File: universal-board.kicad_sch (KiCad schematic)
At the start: 17 parts, among them J1 USB_C_Receptacle, J2 CONN_I2C_GROVE, J3 CONN_WS2812, SW1 SW_RESET, U1 USBLC6-2SC6, U2 USBLC6-2SC6, U3 ESP32-S3-WROOM-1, U4 AMS1117-3.3

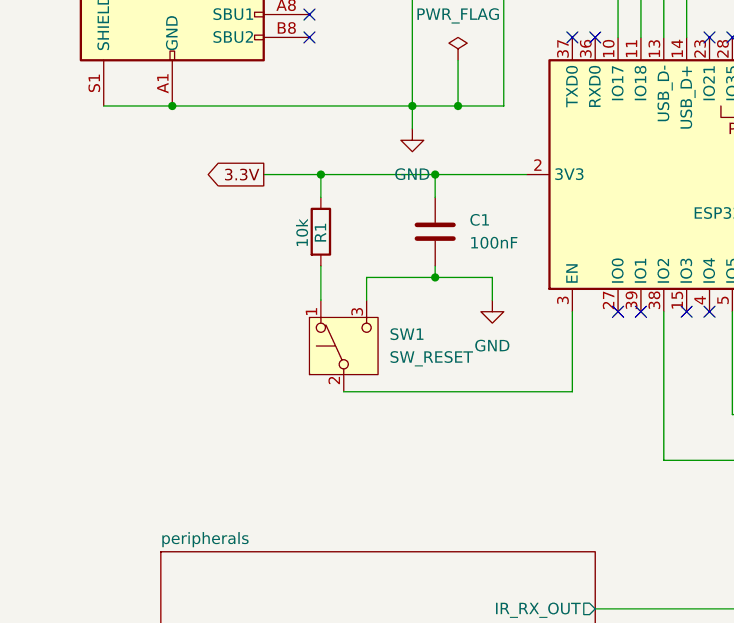
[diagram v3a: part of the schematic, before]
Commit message: Added capacitor for ESP32/EN pin
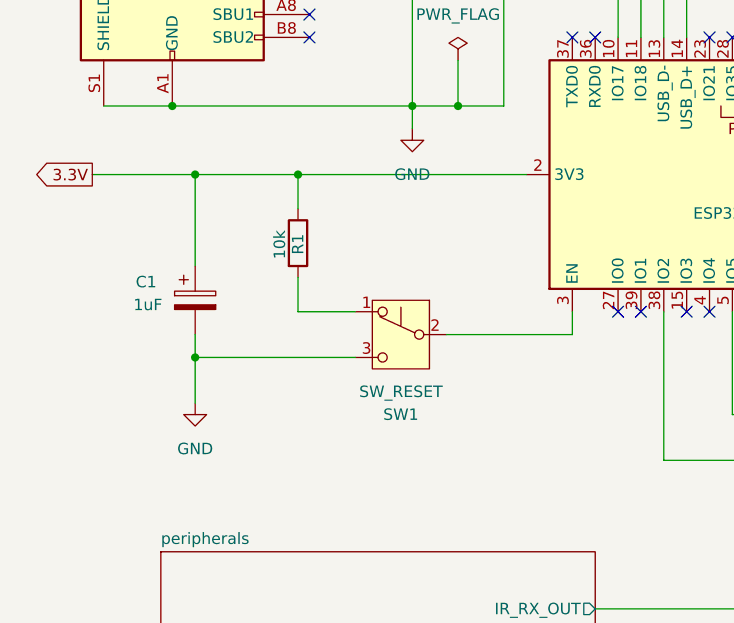
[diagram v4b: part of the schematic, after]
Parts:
- removed C1: 100nF, symbol Device:C
- added C1: 1uF, symbol Device:C_Polarized
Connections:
- net 3.3V: now also C1.1
- net GND: now also C1.2
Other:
- moved on the sheet: R1, SW1

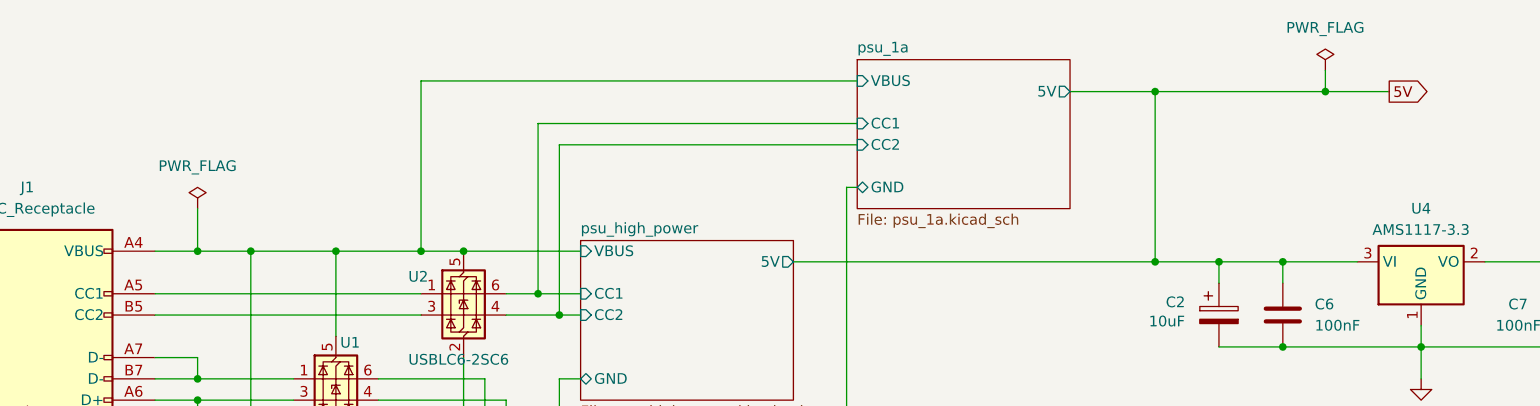
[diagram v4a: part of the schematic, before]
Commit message: Moved some components around for better readability.
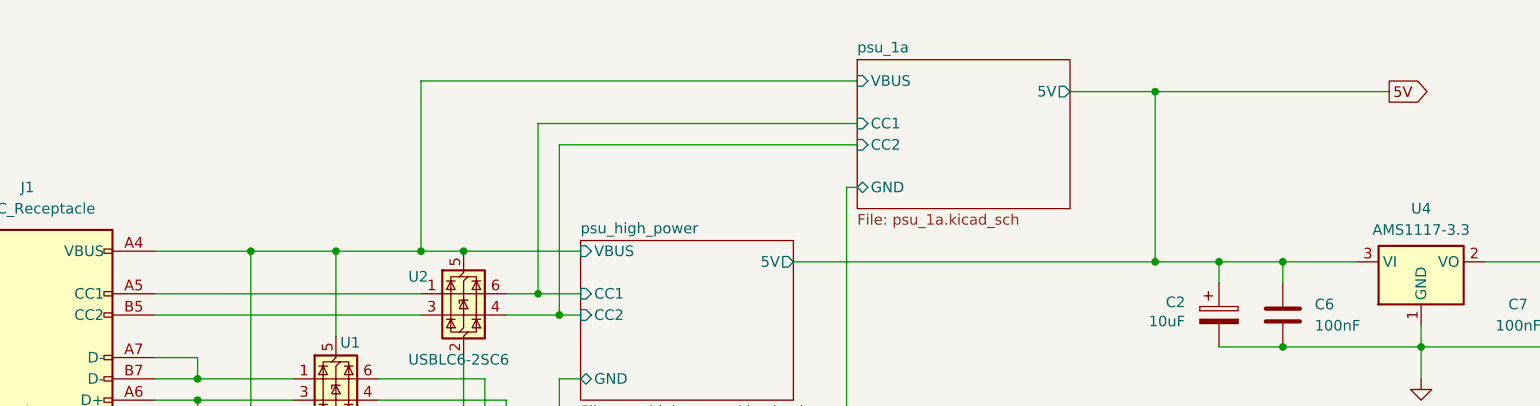
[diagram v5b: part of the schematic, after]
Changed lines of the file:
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@@
-	)
-	(junction
-		(at 185.42 21.59)
-		(diameter 0)
-		(color 0 0 0 0)
 	)
 	(junction
@@
 	)
 	(junction
-		(at 50.8 40.64)
-		(diameter 0)
-		(color 0 0 0 0)
-	)
-	(junction
 		(at 50.8 55.88)
 		(diameter 0)
@@
 	(wire
 		(pts
-			(xy 185.42 21.59) (xy 193.04 21.59)
+			(xy 165.1 21.59) (xy 193.04 21.59)
 		)
 		(stroke
@@
 	(wire
 		(pts
-			(xy 50.8 40.64) (xy 57.15 40.64)
-		)
-		(stroke
-			(width 0)
-			(type default)
-		)
-	)
-	(wire
-		(pts
 			(xy 154.94 21.59) (xy 165.1 21.59)
 		)
@@
 	(wire
 		(pts
-			(xy 50.8 35.56) (xy 50.8 40.64)
-		)
-		(stroke
-			(width 0)
-			(type default)
-		)
-	)
-	(wire
-		(pts
 			(xy 77.47 173.99) (xy 102.87 173.99)
 		)
@@
 	(wire
 		(pts
-			(xy 185.42 19.05) (xy 185.42 21.59)
-		)
-		(stroke
-			(width 0)
-			(type default)
-		)
-	)
-	(wire
-		(pts
 			(xy 91.44 25.4) (xy 91.44 45.72)
 		)
@@
 	(wire
 		(pts
-			(xy 50.8 40.64) (xy 45.72 40.64)
+			(xy 45.72 40.64) (xy 57.15 40.64)
 		)
 		(stroke
@@
 		(pts
 			(xy 33.02 134.62) (xy 50.8 134.62)
-		)
-		(stroke
-			(width 0)
-			(type default)
-		)
-	)
-	(wire
-		(pts
-			(xy 165.1 21.59) (xy 185.42 21.59)
 		)
 		(stroke
@@
 	)
 	(symbol
-		(lib_id "power:PWR_FLAG")
-		(at 185.42 19.05 0)
-		(unit 1)
-		(exclude_from_sim no)
-		(in_bom yes)
-		(on_board yes)
-		(dnp no)
-		(fields_autoplaced yes)
-		(property "Reference" "#FLG03"
-			(at 185.42 17.145 0)
-			(effects
-				(font
-					(size 1.27 1.27)
-				)
-				(hide yes)
-			)
-		)
-		(property "Value" "PWR_FLAG"
-			(at 185.42 13.97 0)
-			(effects
-				(font
-					(size 1.27 1.27)
-				)
-			)
-		)
-		(property "Footprint" ""
-			(at 185.42 19.05 0)
-			(effects
-				(font
-					(size 1.27 1.27)
-				)
-				(hide yes)
-			)
-		)
-		(property "Datasheet" "~"
-			(at 185.42 19.05 0)
-			(effects
-				(font
-					(size 1.27 1.27)
-				)
-				(hide yes)
-			)
-		)
-		(property "Description" "Special symbol for telling ERC where power comes from"
-			(at 185.42 19.05 0)
-			(effects
-				(font
-					(size 1.27 1.27)
-				)
-				(hide yes)
-			)
-		)
-		(pin "1"
-		)
-		(instances
-			(project ""
-				(path "/64404f27-cfd6-41d9-8edb-810ebab8cc14"
-					(reference "#FLG03")
-					(unit 1)
-				)
-			)
-		)
-	)
-	(symbol
 		(lib_id "Connector_Generic:Conn_01x03")
 		(at 163.83 173.99 0)
@@
 					(unit 1)
 				)
-			)
-		)
-	)
-	(symbol
-		(lib_id "power:PWR_FLAG")
-		(at 50.8 35.56 0)
-		(unit 1)
-		(exclude_from_sim no)
-		(in_bom yes)
-		(on_board yes)
-		(dnp no)
-		(fields_autoplaced yes)
-		(property "Reference" "#FLG01"
-			(at 50.8 33.655 0)
-			(effects
-				(font
-					(size 1.27 1.27)
-				)
-				(hide yes)
-			)
-		)
-		(property "Value" "PWR_FLAG"
-			(at 50.8 30.48 0)
-			(effects
-				(font
-					(size 1.27 1.27)
-				)
-			)
-		)
-		(property "Footprint" ""
-			(at 50.8 35.56 0)
-			(effects
-				(font
-					(size 1.27 1.27)
-				)
-				(hide yes)
-			)
-		)
-		(property "Datasheet" "~"
-			(at 50.8 35.56 0)
-			(effects
-				(font
-					(size 1.27 1.27)
-				)
-				(hide yes)
-			)
-		)
-		(property "Description" "Special symbol for telling ERC where power comes from"
-			(at 50.8 35.56 0)
-			(effects
-				(font
-					(size 1.27 1.27)
-				)
-				(hide yes)
-			)
-		)
-		(pin "1"
-		)
-		(instances
-			(project ""
-				(path "/64404f27-cfd6-41d9-8edb-810ebab8cc14"
-					(reference "#FLG01")
-					(unit 1)
-				)

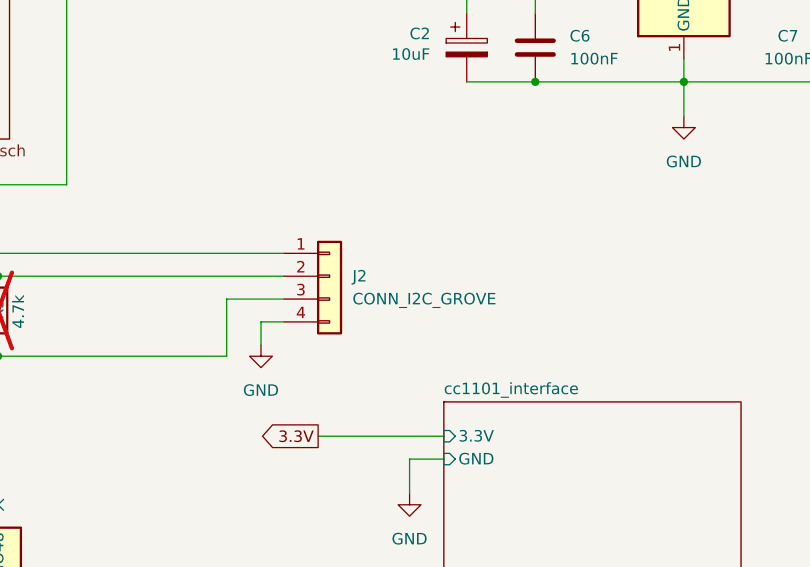
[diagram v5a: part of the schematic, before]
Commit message: Flipped grove connector around
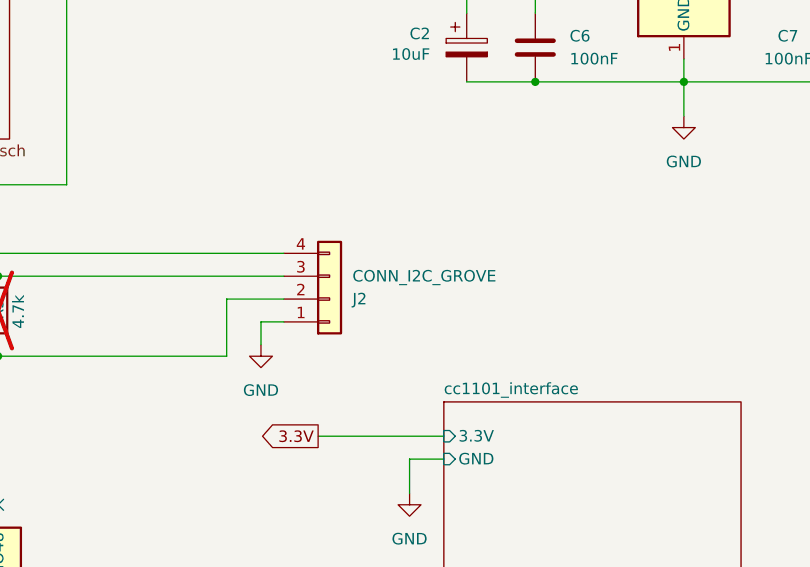
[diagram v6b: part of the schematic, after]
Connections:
- net 3.3V: now also J2.2 (Pin_2); no longer J2.3 (Pin_3)
- net GND: now also J2.1 (Pin_1); no longer J2.4 (Pin_4)
- net at R2.1, U3.10 (IO17): now also J2.4 (Pin_4); no longer J2.1 (Pin_1)
- net at R3.1, U3.11 (IO18): now also J2.3 (Pin_3); no longer J2.2 (Pin_2)
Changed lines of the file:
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@@
 	(symbol
 		(lib_id "Connector_Generic:Conn_01x04")
-		(at 157.48 73.66 0)
+		(at 157.48 76.2 0)
+		(mirror x)
 		(unit 1)
 		(exclude_from_sim no)
@@
 		(on_board yes)
 		(dnp no)
-		(fields_autoplaced yes)
 		(property "Reference" "J2"
-			(at 160.02 73.6599 0)
+			(at 160.02 76.2001 0)
 			(effects
 				(font
@@
 		)
 		(property "Value" "CONN_I2C_GROVE"
-			(at 160.02 76.1999 0)
+			(at 160.02 73.6601 0)
 			(effects
 				(font
@@
 		)
 		(property "Footprint" ""
-			(at 157.48 73.66 0)
+			(at 157.48 76.2 0)
 			(effects
 				(font
@@
 		)
 		(property "Datasheet" "~"
-			(at 157.48 73.66 0)
+			(at 157.48 76.2 0)
 			(effects
 				(font
@@
 		)
 		(property "Description" "Generic connector, single row, 01x04, script generated (kicad-library-utils/schlib/autogen/connector/)"
-			(at 157.48 73.66 0)
+			(at 157.48 76.2 0)
 			(effects
 				(font

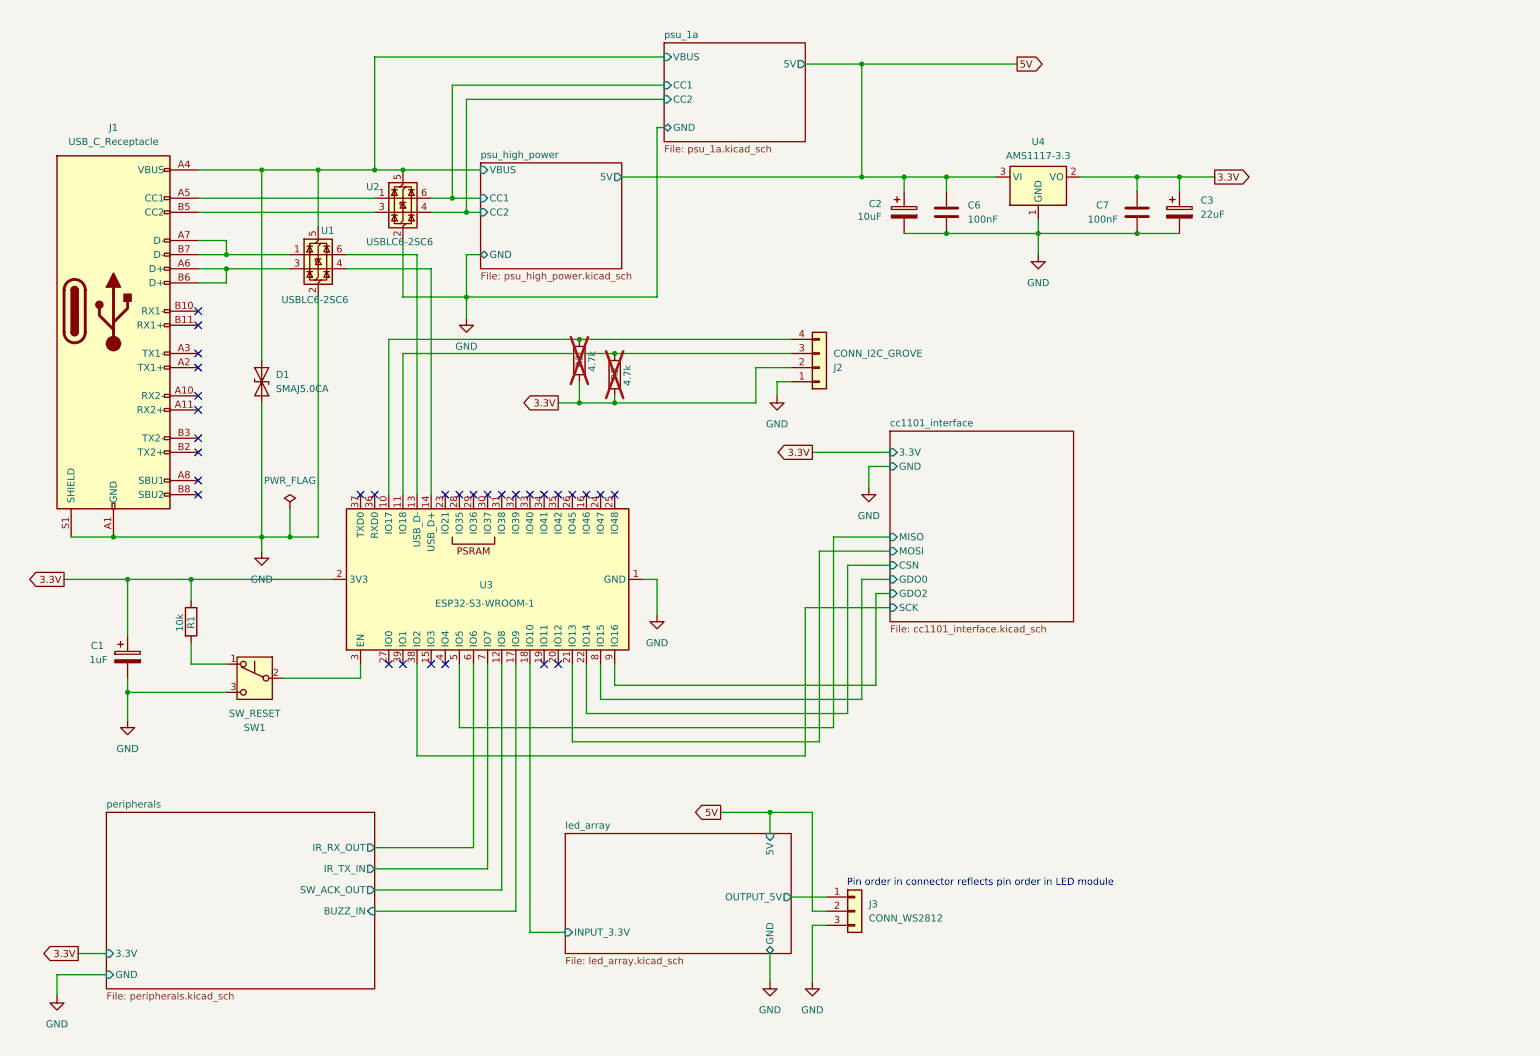
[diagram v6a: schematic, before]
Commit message: Reorganized board to be on one sheet.
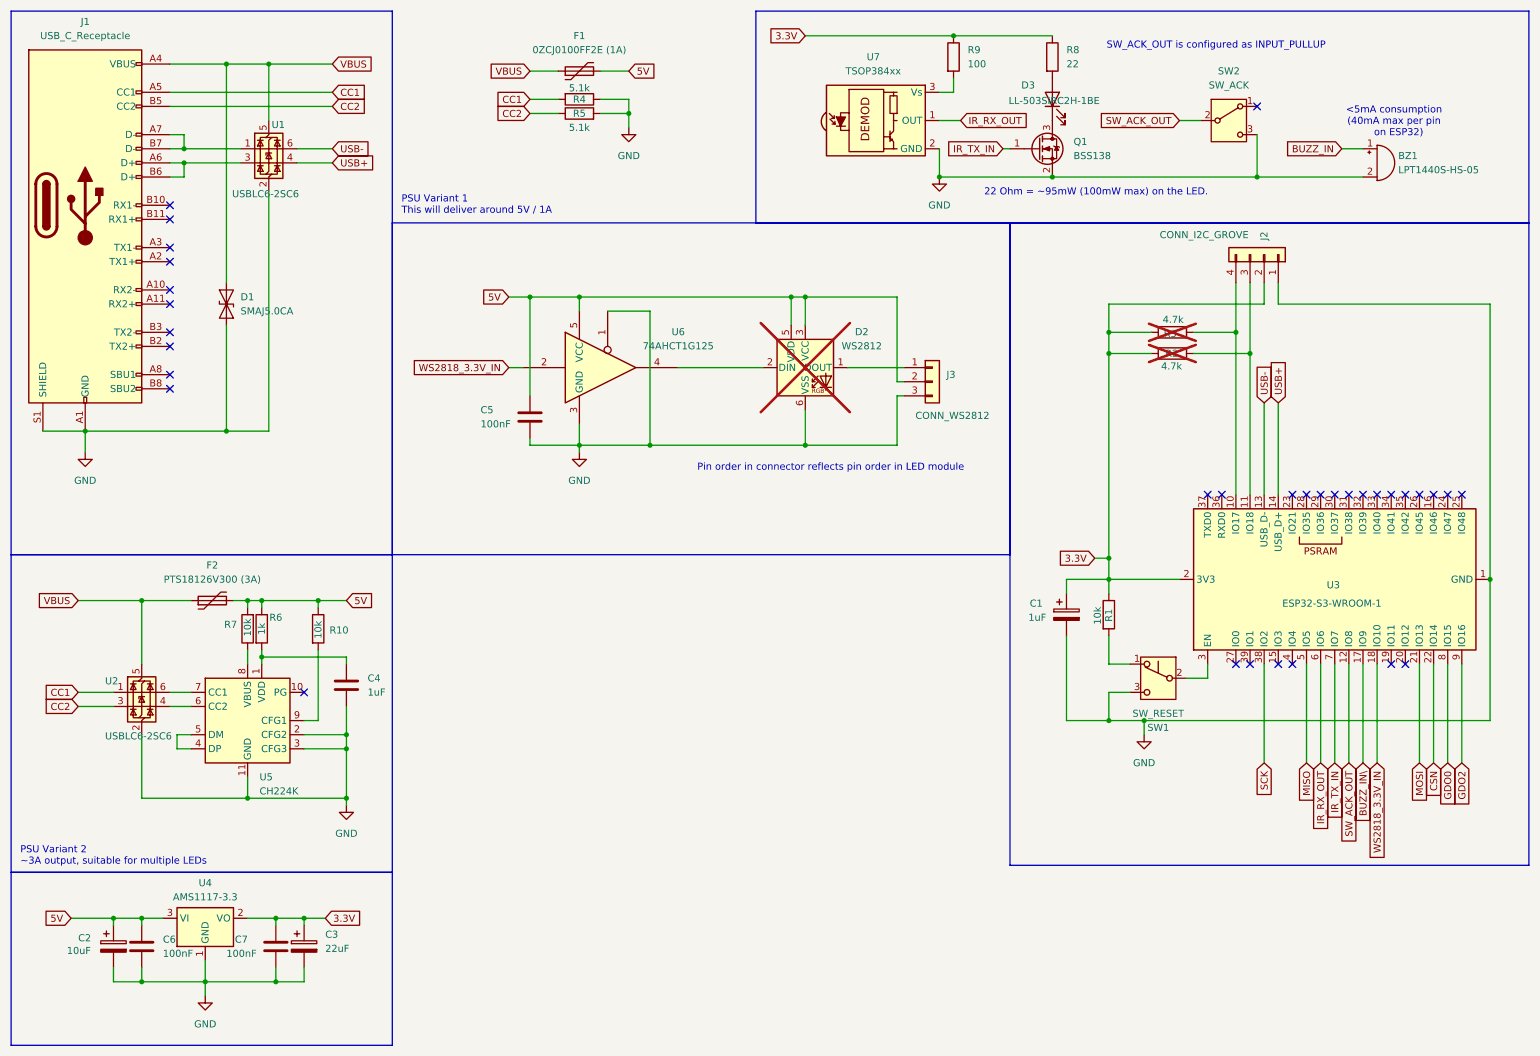
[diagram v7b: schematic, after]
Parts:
- added BZ1: LPT1440S-HS-05, symbol Device:Buzzer
- added C4: 1uF, symbol Device:C
- added C5: 100nF, symbol Device:C
- added D2: WS2812, LED_SMD:LED_WS2812_PLCC6_5.0x5.0mm_P1.6mm, symbol LED:WS2812
- added D3: LL-503SIRC2H-1BE, symbol Device:LED
- added F1: 0ZCJ0100FF2E (1A), symbol Device:Polyfuse
- added F2: PTS18126V300 (3A), symbol Device:Polyfuse
- added Q1: BSS138, Package_TO_SOT_SMD:SOT-23, symbol Transistor_FET:BSS138
- added R10, R7: 10k, symbol Device:R
- added R4, R5: 5.1k, symbol Device:R
- added R6: 1k, symbol Device:R
- added R8: 22, symbol Device:R
- added R9: 100, symbol Device:R
- added SW2: SW_ACK, symbol Switch:SW_SPDT
- added U5: CH224K, Package_SO:SSOP-10-1EP_3.9x4.9mm_P1mm_EP2.1x3.3mm, symbol Interface_USB:CH224K
- added U6: 74AHCT1G125, symbol 74xGxx:74AHCT1G125
- added U7: TSOP384xx, OptoDevice:Vishay_MINICAST-3Pin, symbol Interface_Optical:TSOP384xx
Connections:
- net 3.3V: now also R3.1, R8.1, R9.1; no longer R3.2
- net 5V: now also C5.1, D2.3 (VCC), D2.5 (VDD), F1.2, F2.2, R10.1, R6.1, R7.2, U6.5 (VCC)
- net GND: now also BZ1.2 (-), C4.2, C5.2, D2.6 (VSS), Q1.2 (S), R4.1, R5.2, SW2.3 (C), U5.11 (GND), U5.2 (CFG2), U5.3 (CFG3), U6.1, U6.3 (GND), U7.2 (GND)
- net CC1: now reaches J1.A5 (CC1), U2.1 (I/O1)
- net CC1: now also R4.2
- net CC2: now reaches J1.B5 (CC2), U2.3 (I/O2)
- net CC2: now also R5.1
- net at J2.3 (Pin_3), U3.11 (IO18): now also R2.1; no longer R3.1
- net at J2.4 (Pin_4), U3.10 (IO17): now also R3.2; no longer R2.1
- net USB+: now reaches U1.4 (I/O2), U3.14 (USB_D+)
- net USB-: now reaches U1.6 (I/O1), U3.13 (USB_D-)
- net cc1101_interface/CSN renamed CSN
- net cc1101_interface/GDO0 renamed GDO0
- net cc1101_interface/GDO2 renamed GDO2
- net cc1101_interface/MISO renamed MISO
- net cc1101_interface/MOSI renamed MOSI
- net cc1101_interface/SCK renamed SCK
- net led_array/INPUT_3.3V renamed WS2818_3.3V_IN
- net WS2818_3.3V_IN: now also U6.2
- net led_array/OUTPUT_5V: no longer names the net of J3.1 (Pin_1)
- net led_array/OUTPUT_5V: now also D2.1 (DOUT)
- net peripherals/BUZZ_IN renamed BUZZ_IN\
- net peripherals/IR_RX_OUT renamed IR_RX_OUT
- net IR_RX_OUT: now also U7.1 (OUT)
- net peripherals/IR_TX_IN renamed IR_TX_IN
- net IR_TX_IN: now also Q1.1 (G)
- net peripherals/SW_ACK_OUT renamed SW_ACK_OUT
- net SW_ACK_OUT: now also SW2.2 (B)
- net psu_1a/CC1: no longer names the net of U2.6 (I/O1)
- net psu_1a/CC1: now also U5.7 (CC1)
- net psu_1a/CC2: no longer names the net of U2.4 (I/O2)
- net psu_1a/CC2: now also U5.6 (CC2)
- net psu_1a/VBUS renamed VBUS
- net VBUS: now also F1.1, F2.1
- new net: D3.1 (K), Q1.3 (D)
- new net: D3.2 (A), R8.2
- new net: C4.1, R6.2, U5.1 (VDD)
- new net: U5.4 (DP), U5.5 (DM)
- new net: R7.1, U5.8 (VBUS)
- new net: R10.2, U5.9 (CFG1)
- new net: D2.2 (DIN), U6.4
- new net: R9.2, U7.3 (Vs)
- new net BUZZ_IN: BZ1.1 (+)
- no-connect marks 31 -> 33
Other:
- removed sheet cc1101_interface
- removed sheet led_array
- removed sheet peripherals
- removed sheet psu_1a
- removed sheet psu_high_power
- note added: "22 Ohm = ~95mW (100mW max) on the LED."
- note added: "<5mA consumption (40mA max per pin on ESP32)"
- note added: "PSU Variant 1 This will deliver around 5V / 1A"
- note added: "PSU Variant 2 ~3A output, suitable for multiple LEDs"
- note added: "SW_ACK_OUT is configured as INPUT_PULLUP"
- moved on the sheet: C1, C2, C3, C6, C7, D1, J1, J2, J3, R1, R2, R3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
